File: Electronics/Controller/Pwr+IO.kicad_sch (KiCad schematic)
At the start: 27 parts, among them J401 IO, Q401 AO3400A, Q402 AO3400A, Q403 AO3400A, U401 MCP16301

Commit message: PDF Update
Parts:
- C403: value 100uF -> 68uF; Voltage 16V -> 35V
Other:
- company: (none) -> findersee.fi
- title: (none) -> MQTT Output Controller
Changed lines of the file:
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@@
 (kicad_sch (version 20230121) (generator eeschema)
   (paper "A3")
+  (title_block
+    (title "MQTT Output Controller")
+    (date "2023-09-16")
+    (rev "1.0")
+    (company "findersee.fi")
+  )
   (junction (at 110.49 34.29) (diameter 0) (color 0 0 0 0)
   )
@@
       (effects (font (size 1.27 1.27)) (justify left))
     )
-    (property "Value" "100uF" (at 352.171 113.4183 0)
+    (property "Value" "68uF" (at 352.171 113.4183 0)
       (effects (font (size 1.27 1.27)) (justify left))
     )
@@
       (effects (font (size 1.27 1.27)) hide)
     )
-    (property "Voltage" "16V" (at 352.171 115.57 0)
+    (property "Voltage" "35V" (at 352.171 115.57 0)
       (effects (font (size 1 1)) (justify left))
     )

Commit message: Manufacturing commit 2
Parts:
- D303: footprint LED_SMD:LED_0805_2012Metric -> LED_SMD:LED_0603_1608Metric; symbol Device:LED_Filled -> Device:LED_Small_Filled
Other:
- moved on the sheet: D303
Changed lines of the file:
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@@
     (stroke (width 0) (type default))
   )
-  (wire (pts (xy 148.59 44.45) (xy 148.59 45.72))
+  (wire (pts (xy 148.59 41.91) (xy 148.59 45.72))
     (stroke (width 0) (type default))
   )
@@
     )
   )
-  (symbol (lib_id "Device:LED_Filled") (at 148.59 40.64 270) (mirror x) (unit 1)
+  (symbol (lib_id "Device:LED_Small_Filled") (at 148.59 39.37 270) (mirror x) (unit 1)
     (in_bom yes) (on_board yes) (dnp no)
-    (property "Reference" "D303" (at 151.13 38.1 90)
+    (property "Reference" "D303" (at 151.13 36.83 90)
       (effects (font (size 1.27 1.27)))
     )
-    (property "Value" "White" (at 152.4 40.64 90)
+    (property "Value" "White" (at 152.4 41.91 90)
       (effects (font (size 1.27 1.27)))
     )
-    (property "Footprint" "LED_SMD:LED_0805_2012Metric" (at 148.59 40.64 0)
+    (property "Footprint" "LED_SMD:LED_0603_1608Metric" (at 148.59 39.37 90)
       (effects (font (size 1.27 1.27)) hide)
     )
-    (property "Datasheet" "~" (at 148.59 40.64 0)
+    (property "Datasheet" "~" (at 148.59 39.37 90)
       (effects (font (size 1.27 1.27)) hide)
     )

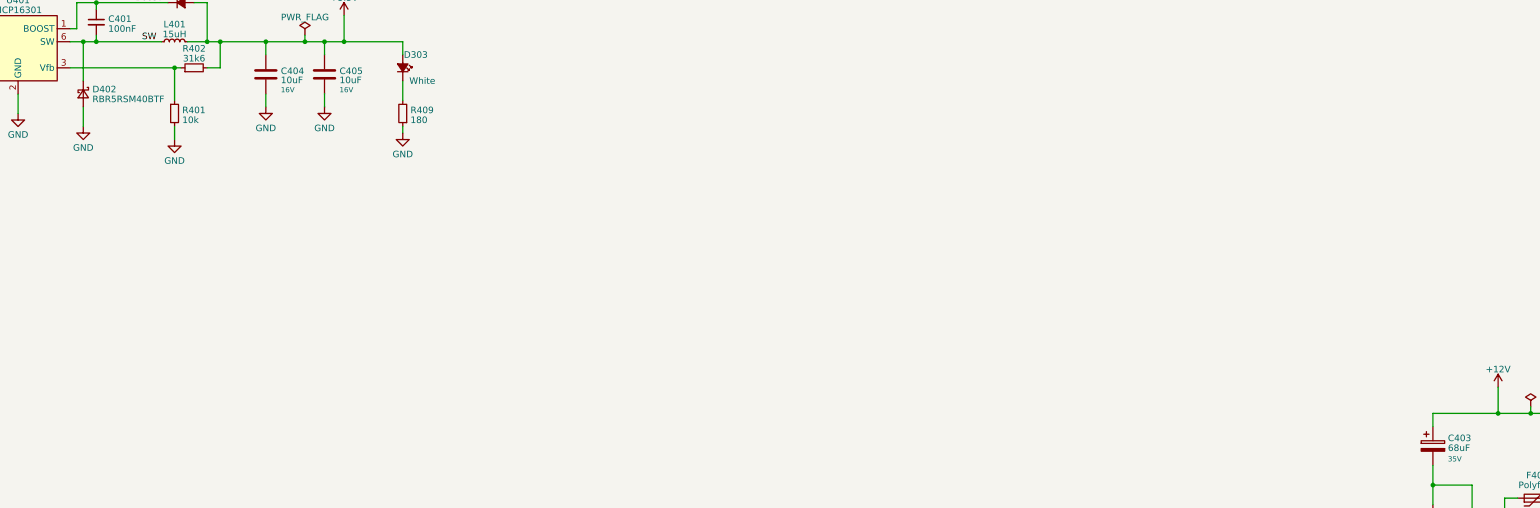
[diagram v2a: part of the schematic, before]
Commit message: Pin goof fix
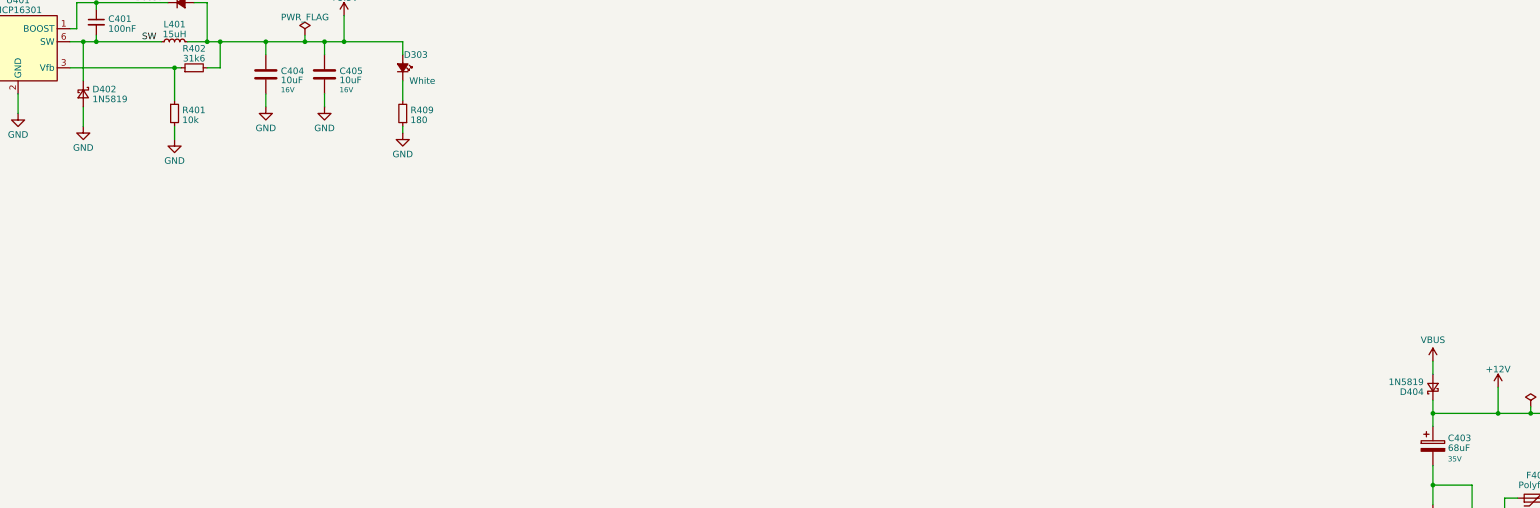
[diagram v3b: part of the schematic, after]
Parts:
- added D404: 1N5819, Diode_SMD:D_SOD-123, symbol Device:D_Schottky_Small
- D402: value RBR5RSM40BTF -> 1N5819
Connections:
- net +12V: now also D404.1 (K)
- new net VBUS: D404.2 (A)
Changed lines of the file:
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@@
   (junction (at 292.1 173.99) (diameter 0) (color 0 0 0 0)
   )
+  (junction (at 349.25 106.68) (diameter 0) (color 0 0 0 0)
+  )
   (junction (at 121.92 34.29) (diameter 0) (color 0 0 0 0)
   )
@@
     (stroke (width 0) (type default))
   )
+  (wire (pts (xy 349.25 96.52) (xy 349.25 99.06))
+    (stroke (width 0) (type default))
+  )
   (wire (pts (xy 361.95 106.68) (xy 368.3 106.68))
     (stroke (width 0) (type default))
@@
   )
   (wire (pts (xy 377.19 138.43) (xy 363.22 138.43))
+    (stroke (width 0) (type default))
+  )
+  (wire (pts (xy 349.25 104.14) (xy 349.25 106.68))
     (stroke (width 0) (type default))
   )
@@
       (effects (font (size 1.27 1.27)) (justify left))
     )
-    (property "Value" " RBR5RSM40BTF" (at 88.138 45.4733 90)
+    (property "Value" "1N5819" (at 88.138 45.4733 90)
       (effects (font (size 1.27 1.27)) (justify left))
     )
@@
     )
   )
+  (symbol (lib_id "Device:D_Schottky_Small") (at 349.25 101.6 90) (unit 1)
+    (in_bom yes) (on_board yes) (dnp no)
+    (property "Reference" "D404" (at 347.472 102.4977 90)
+      (effects (font (size 1.27 1.27)) (justify left))
+    )
+    (property "Value" "1N5819" (at 347.472 100.5767 90)
+      (effects (font (size 1.27 1.27)) (justify left))
+    )
+    (property "Footprint" "Diode_SMD:D_SOD-123" (at 349.25 101.6 90)
+      (effects (font (size 1.27 1.27)) hide)
+    )
+    (property "Datasheet" "~" (at 349.25 101.6 90)
+      (effects (font (size 1.27 1.27)) hide)
+    )
+    (pin "1")
+    (pin "2")
+    (instances
+      (project "Controller"
+        (path "/a2ea94cb-4178-4727-9ac9-0e597b4a505d/7516d84f-d298-4f48-8b5d-a736b2d19d1b"
+          (reference "D404") (unit 1)
+        )
+      )
+    )
+  )
   (symbol (lib_id "power:PWR_FLAG") (at 129.54 33.02 0) (unit 1)
     (in_bom yes) (on_board yes) (dnp no) (fields_autoplaced)
@@
         )
       )
+    )
+  )
+  (symbol (lib_id "power:VBUS") (at 349.25 96.52 0) (unit 1)
+    (in_bom yes) (on_board yes) (dnp no) (fields_autoplaced)
+    (property "Reference" "#PWR0404" (at 349.25 100.33 0)
+      (effects (font (size 1.27 1.27)) hide)
+    )
+    (property "Value" "VBUS" (at 349.25 92.3869 0)
+      (effects (font (size 1.27 1.27)))
+    )
+    (property "Footprint" "" (at 349.25 96.52 0)
+      (effects (font (size 1.27 1.27)) hide)
+    )
+    (property "Datasheet" "" (at 349.25 96.52 0)
+      (effects (font (size 1.27 1.27)) hide)
+    )
+    (pin "1")
+    (instances
+      (project "Controller"
+        (path "/a2ea94cb-4178-4727-9ac9-0e597b4a505d/7516d84f-d298-4f48-8b5d-a736b2d19d1b"
+          (reference "#PWR0404") (unit 1)
+        )
+      )

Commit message: Added library Fixed layout bugs Software improvements
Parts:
- C402, C404, C405: Package (none) -> 0805
- C403: Package (none) -> 6.3x5.8
- H401, H402: footprint MountingHole:MountingHole_3.2mm_M3_DIN965 -> MountingHole:MountingHole_2.5mm
- R403, R404, R411: symbol Device:R_Small -> Resistors_0402:RESC_0402_10k; Package (none) -> 0402
- R405, R406, R410: symbol Device:R_Small -> Resistors_0402:RESC_0402_0R; Package (none) -> 0402
- R409: value 180 -> 187R; symbol Device:R_Small -> Resistors_0402:RESC_0402_187R; Package (none) -> 0402
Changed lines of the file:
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@@
     )
   )
-  (symbol (lib_id "Device:R_Small") (at 148.59 48.26 180) (unit 1)
+  (symbol (lib_id "Resistors_0402:RESC_0402_187R") (at 148.59 48.26 180) (unit 1)
     (in_bom yes) (on_board yes) (dnp no) (fields_autoplaced)
     (property "Reference" "R409" (at 150.0886 47.6163 0)
       (effects (font (size 1.27 1.27)) (justify right))
     )
-    (property "Value" "180" (at 150.0886 49.5373 0)
+    (property "Value" "187R" (at 150.0886 49.5373 0)
       (effects (font (size 1.27 1.27)) (justify right))
     )
@@
     (property "Datasheet" "~" (at 148.59 48.26 0)
       (effects (font (size 1.27 1.27)) hide)
+    )
+    (property "Package" "0402" (at 149.86 49.53 0)
+      (effects (font (size 0.8 0.8)) hide)
     )
     (pin "1")
@@
     (property "Voltage" "16V" (at 124.841 43.6606 0)
       (effects (font (size 1 1)) (justify left))
+    )
+    (property "Package" "0805" (at 121.92 40.64 0)
+      (effects (font (size 1.27 1.27)) hide)
     )
     (pin "1")
@@
     )
   )
-  (symbol (lib_id "Device:R_Small") (at 292.1 177.8 0) (mirror y) (unit 1)
+  (symbol (lib_id "Resistors_0402:RESC_0402_10k") (at 292.1 177.8 0) (mirror y) (unit 1)
     (in_bom yes) (on_board yes) (dnp no)
     (property "Reference" "R403" (at 290.6014 177.1563 0)
@@
     )
     (property "Value" "10k" (at 290.6014 179.0773 0)
-      (effects (font (size 1.27 1.27)) (justify left) hide)
+      (effects (font (size 1.27 1.27)) (justify left))
     )
     (property "Footprint" "Resistor_SMD:R_0402_1005Metric" (at 292.1 177.8 0)
@@
       (effects (font (size 1.27 1.27)) hide)
     )
+    (property "Package" "0402" (at 293.37 176.53 0)
+      (effects (font (size 0.8 0.8)) hide)
+    )
     (pin "1")
     (pin "2")
@@
       (effects (font (size 1.27 1.27)) (justify left))
     )
-    (property "Footprint" "MountingHole:MountingHole_3.2mm_M3_DIN965" (at 38.735 262.255 0)
+    (property "Footprint" "MountingHole:MountingHole_2.5mm" (at 38.735 262.255 0)
       (effects (font (size 1.27 1.27)) hide)
     )
@@
     )
   )
-  (symbol (lib_id "Device:R_Small") (at 283.21 173.99 90) (unit 1)
+  (symbol (lib_id "Resistors_0402:RESC_0402_0R") (at 283.21 173.99 90) (unit 1)
     (in_bom yes) (on_board yes) (dnp no) (fields_autoplaced)
     (property "Reference" "R405" (at 283.21 170.2435 90)
@@
     (property "Datasheet" "~" (at 283.21 173.99 0)
       (effects (font (size 1.27 1.27)) hide)
+    )
+    (property "Package" "0402" (at 281.94 175.26 0)
+      (effects (font (size 0.8 0.8)) hide)
     )
     (pin "1")
@@
       (effects (font (size 1 1)) (justify left))
     )
+    (property "Package" "0805" (at 133.35 40.64 0)
+      (effects (font (size 1.27 1.27)) hide)
+    )
     (pin "1")
     (pin "2")
@@
     )
   )
-  (symbol (lib_id "Device:R_Small") (at 331.47 228.6 0) (unit 1)
+  (symbol (lib_id "Resistors_0402:RESC_0402_10k") (at 331.47 228.6 0) (unit 1)
     (in_bom yes) (on_board yes) (dnp no) (fields_autoplaced)
     (property "Reference" "R411" (at 332.9686 227.9563 0)
@@
       (effects (font (size 1.27 1.27)) hide)
     )
+    (property "Package" "0402" (at 330.2 227.33 0)
+      (effects (font (size 0.8 0.8)) hide)
+    )
     (pin "1")
     (pin "2")
@@
     )
   )
-  (symbol (lib_id "Device:R_Small") (at 308.61 198.12 90) (unit 1)
+  (symbol (lib_id "Resistors_0402:RESC_0402_0R") (at 308.61 198.12 90) (unit 1)
     (in_bom yes) (on_board yes) (dnp no) (fields_autoplaced)
     (property "Reference" "R406" (at 308.61 194.3735 90)
@@
     (property "Datasheet" "~" (at 308.61 198.12 0)
       (effects (font (size 1.27 1.27)) hide)
+    )
+    (property "Package" "0402" (at 307.34 199.39 0)
+      (effects (font (size 0.8 0.8)) hide)
     )
     (pin "1")
@@
       (effects (font (size 1 1)) (justify left))
     )
+    (property "Package" "0805" (at 52.07 38.1 0)
+      (effects (font (size 1.27 1.27)) hide)
+    )
     (pin "1")
     (pin "2")
@@
     )
   )
-  (symbol (lib_id "Device:R_Small") (at 316.23 201.93 0) (mirror y) (unit 1)
+  (symbol (lib_id "Resistors_0402:RESC_0402_10k") (at 316.23 201.93 0) (mirror y) (unit 1)
     (in_bom yes) (on_board yes) (dnp no)
     (property "Reference" "R404" (at 314.7314 201.2863 0)
@@
     (property "Datasheet" "~" (at 316.23 201.93 0)
       (effects (font (size 1.27 1.27)) hide)
+    )
+    (property "Package" "0402" (at 317.5 200.66 0)
+      (effects (font (size 0.8 0.8)) hide)
     )
     (pin "1")
@@
       (effects (font (size 1 1)) (justify left))
     )
+    (property "Package" "6.3x5.8" (at 349.25 113.03 0)
+      (effects (font (size 1.27 1.27)) hide)
+    )
     (pin "1")
     (pin "2")
@@
       (effects (font (size 1.27 1.27)) (justify left))
     )
-    (property "Footprint" "MountingHole:MountingHole_3.2mm_M3_DIN965" (at 38.735 267.97 0)
+    (property "Footprint" "MountingHole:MountingHole_2.5mm" (at 38.735 267.97 0)
       (effects (font (size 1.27 1.27)) hide)
     )
@@
     )
   )
-  (symbol (lib_id "Device:R_Small") (at 323.85 224.79 90) (unit 1)
+  (symbol (lib_id "Resistors_0402:RESC_0402_0R") (at 323.85 224.79 90) (unit 1)
     (in_bom yes) (on_board yes) (dnp no) (fields_autoplaced)
     (property "Reference" "R410" (at 323.85 221.0435 90)
@@
       (effects (font (size 1.27 1.27)) hide)
     )
-    (pin "1")
+    (property "Package" "0402" (at 322.58 226.06 0)
+      (effects (font (size 0.8 0.8)) hide)
+    )
+    (pin "1")

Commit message: Schematic and Layout update
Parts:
- removed D401: 1N4148, Diode_SMD:D_SOD-123, symbol Device:D_Small_Filled
- removed FB302: 120R, Resistor_SMD:R_0805_2012Metric, symbol Device:FerriteBead_Small
- added D401, D405: 1N5819, Diode_SMD:D_SOD-123, symbol Device:D_Schottky_Small
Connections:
- net +12V: now also D405.2 (A)
- net +3.3V: now also D401.2 (A)
- net Boost: now also D401.1 (K)
- net at C402.1, U401.4 (EN), U401.5 (Vin): now also D405.1 (K)
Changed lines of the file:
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@@
-    )
-  )
-  (symbol (lib_id "Device:D_Small_Filled") (at 105.41 26.67 0) (unit 1)
-    (in_bom yes) (on_board yes) (dnp no) (fields_autoplaced)
-    (property "Reference" "D401" (at 105.41 22.6441 0)
-      (effects (font (size 1.27 1.27)))
-    )
-    (property "Value" "1N4148" (at 105.41 24.5651 0)
-      (effects (font (size 1.27 1.27)))
-    )
-    (property "Footprint" "Diode_SMD:D_SOD-123" (at 105.41 26.67 90)
-      (effects (font (size 1.27 1.27)) hide)
-    )
-    (property "Datasheet" "~" (at 105.41 26.67 90)
-      (effects (font (size 1.27 1.27)) hide)
-    )
-    (property "Sim.Device" "D" (at 105.41 26.67 0)
-      (effects (font (size 1.27 1.27)) hide)
-    )
-    (property "Sim.Pins" "1=K 2=A" (at 105.41 26.67 0)
-      (effects (font (size 1.27 1.27)) hide)
-    )
-    (pin "1")
-    (pin "2")
-    (instances
-      (project "Controller"
-        (path "/a2ea94cb-4178-4727-9ac9-0e597b4a505d/7516d84f-d298-4f48-8b5d-a736b2d19d1b"
-          (reference "D401") (unit 1)
-        )
-      )
     )
   )
@@
     )
   )
+  (symbol (lib_id "Device:D_Schottky_Small") (at 105.41 26.67 0) (mirror x) (unit 1)
+    (in_bom yes) (on_board yes) (dnp no)
+    (property "Reference" "D401" (at 105.156 21.5097 0)
+      (effects (font (size 1.27 1.27)))
+    )
+    (property "Value" "1N5819" (at 105.156 23.9339 0)
+      (effects (font (size 1.27 1.27)))
+    )
+    (property "Footprint" "Diode_SMD:D_SOD-123" (at 105.41 26.67 90)
+      (effects (font (size 1.27 1.27)) hide)
+    )
+    (property "Datasheet" "~" (at 105.41 26.67 90)
+      (effects (font (size 1.27 1.27)) hide)
+    )
+    (pin "1")
+    (pin "2")
+    (instances
+      (project "Controller"
+        (path "/a2ea94cb-4178-4727-9ac9-0e597b4a505d/7516d84f-d298-4f48-8b5d-a736b2d19d1b"
+          (reference "D401") (unit 1)
+        )
+      )
+    )
+  )
   (symbol (lib_id "Device:L_Small") (at 104.14 34.29 90) (unit 1)
     (in_bom yes) (on_board yes) (dnp no) (fields_autoplaced)
@@
     )
   )
-  (symbol (lib_id "Device:FerriteBead_Small") (at 43.18 31.75 90) (unit 1)
-    (in_bom yes) (on_board yes) (dnp no) (fields_autoplaced)
-    (property "Reference" "FB302" (at 43.1419 27.0383 90)
-      (effects (font (size 1.27 1.27)))
-    )
-    (property "Value" "120R" (at 43.1419 28.9593 90)
-      (effects (font (size 1.27 1.27)))
-    )
-    (property "Footprint" "Resistor_SMD:R_0805_2012Metric" (at 43.18 33.528 90)
-      (effects (font (size 1.27 1.27)) hide)
-    )
-    (property "Datasheet" "~" (at 43.18 31.75 0)
-      (effects (font (size 1.27 1.27)) hide)
-    )
-    (pin "1")
-    (pin "2")
-    (instances
-      (project "Controller"
-        (path "/a2ea94cb-4178-4727-9ac9-0e597b4a505d/5e10769e-2c76-442d-969e-a77f15adcbc3"
-          (reference "FB302") (unit 1)
-        )
-        (path "/a2ea94cb-4178-4727-9ac9-0e597b4a505d/7516d84f-d298-4f48-8b5d-a736b2d19d1b"
-          (reference "FB401") (unit 1)
-        )
-      )
-    )
-  )
   (symbol (lib_id "Device:D_Schottky_Small") (at 349.25 101.6 90) (unit 1)
     (in_bom yes) (on_board yes) (dnp no)
@@
         )
       )
+    )
+  )
+  (symbol (lib_id "Device:D_Schottky_Small") (at 43.18 31.75 180) (unit 1)
+    (in_bom yes) (on_board yes) (dnp no) (fields_autoplaced)
+    (property "Reference" "D405" (at 43.434 26.5897 0)
+      (effects (font (size 1.27 1.27)))
+    )
+    (property "Value" "1N5819" (at 43.434 29.0139 0)
+      (effects (font (size 1.27 1.27)))
+    )
+    (property "Footprint" "Diode_SMD:D_SOD-123" (at 43.18 31.75 90)
+      (effects (font (size 1.27 1.27)) hide)
+    )
+    (property "Datasheet" "~" (at 43.18 31.75 90)
+      (effects (font (size 1.27 1.27)) hide)
+    )
+    (pin "1")
+    (pin "2")
+    (instances
+      (project "Controller"
+        (path "/a2ea94cb-4178-4727-9ac9-0e597b4a505d/7516d84f-d298-4f48-8b5d-a736b2d19d1b"
+          (reference "D405") (unit 1)
+        )
+      )

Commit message: Improvements
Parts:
- added C406: 10uF, Capacitor_SMD:C_0805_2012Metric, symbol Device:C
- C404, C405: footprint Capacitor_SMD:C_0603_1608Metric -> Capacitor_SMD:C_0805_2012Metric
- D405: value 1N5819 -> SK36A-LTP; footprint Diode_SMD:D_SOD-123 -> Diode_SMD:D_SMA
- renumbered D303 to D403
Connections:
- net +12V: now also C402.1, D405.1 (K), U401.4 (EN), U401.5 (Vin), C406.1; no longer D405.2 (A), J401.7 (Pin_7)
- net GND: now also C406.2
- new net: D405.2 (A), J401.7 (Pin_7)
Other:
- moved on the sheet: C403, D405, F403
